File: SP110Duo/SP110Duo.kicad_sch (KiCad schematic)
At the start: 251 parts, among them SW1 RotaryEncoder_Switch, SW10 Switch w/LED, SW100 Switch w/LED, SW101 Switch w/LED, SW102 Switch w/LED, SW103 Switch w/LED, SW104 Switch w/LED, SW105 Switch w/LED, SW106 Switch w/LED, SW107 Switch w/LED, SW108 Switch w/LED, SW109 Switch w/LED, SW11 Switch w/LED, SW110 Switch w/LED, SW12 Switch w/LED, SW13 Switch w/LED, SW14 Switch w/LED, SW15 Switch w/LED, SW16 Switch w/LED, SW17 Switch w/LED, SW18 Switch w/LED, SW19 Switch w/LED, SW2 Switch w/LED, SW20 Switch w/LED, SW21 Switch w/LED, SW22 Switch w/LED, SW23 Switch w/LED, SW24 Switch w/LED, SW25 Switch w/LED, SW26 Switch w/LED, SW27 Switch w/LED, SW28 Switch w/LED, SW29 Switch w/LED, SW3 Switch w/LED, SW30 Switch w/LED, SW31 Switch w/LED, SW32 Switch w/LED, SW33 Switch w/LED, SW34 Switch w/LED, SW35 Switch w/LED, SW36 Switch w/LED, SW37 Switch w/LED, SW38 Switch w/LED, SW39 Switch w/LED, SW4 Switch w/LED, SW40 Switch w/LED, SW41 Switch w/LED, SW42 Switch w/LED, SW43 Switch w/LED, SW44 Switch w/LED, SW45 Switch w/LED, SW46 Switch w/LED, SW47 Switch w/LED, SW48 Switch w/LED, SW49 Switch w/LED, SW5 Switch w/LED, SW50 Switch w/LED, SW51 Switch w/LED, SW52 Switch w/LED, SW53 Switch w/LED, SW54 Switch w/LED, SW55 Switch w/LED, SW56 Switch w/LED, SW57 Switch w/LED, SW58 Switch w/LED, SW59 Switch w/LED, SW6 Switch w/LED, SW60 Switch w/LED, SW61 RotaryEncoder_Switch, SW62 Switch w/LED, SW63 Switch w/LED, SW64 Switch w/LED, SW65 Switch w/LED, SW66 Switch w/LED, SW67 Switch w/LED, SW68 Switch w/LED, SW69 Switch w/LED, SW7 Switch w/LED, SW70 Switch w/LED, SW71 Switch w/LED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

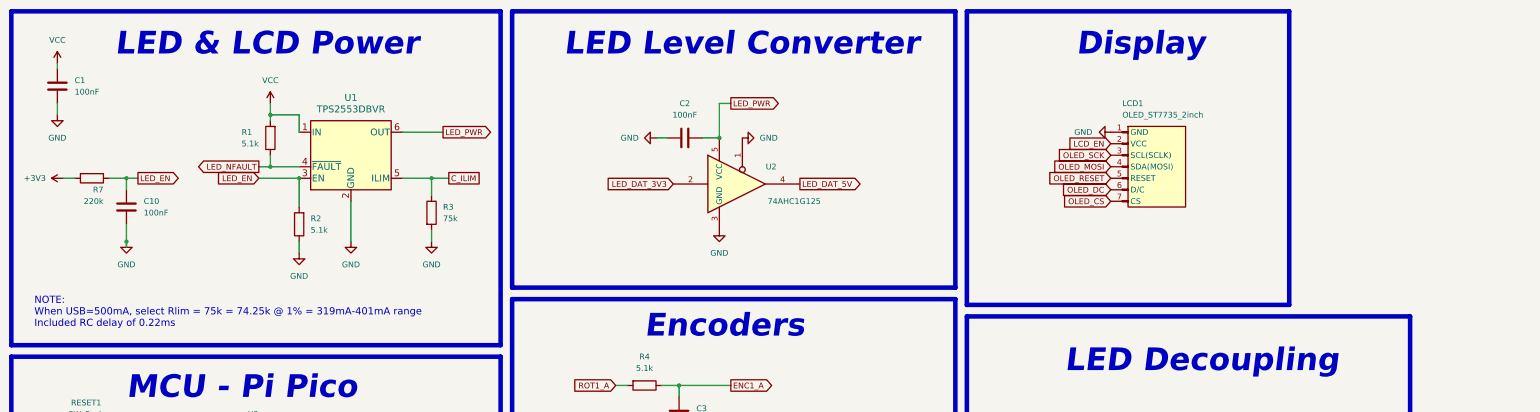
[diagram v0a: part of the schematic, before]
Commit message: Modify diode footprint, add LCD PWR circuit
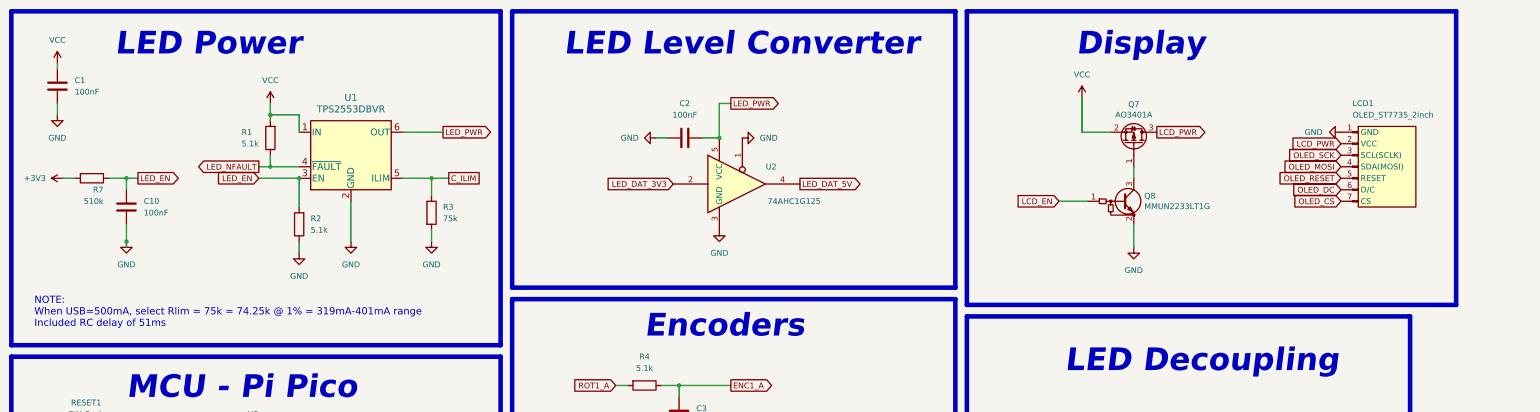
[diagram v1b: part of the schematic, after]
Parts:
- added Q7: AO3401A, Package_TO_SOT_SMD:SOT-23-3, symbol Transistor_FET:AO3401A
- added Q8: MMUN2233LT1G, Package_TO_SOT_SMD:SOT-23-3, symbol Device:Q_NPN_BEC_BRT
- D1, D10, D100, D101, D102, D103, D104, D105, D106, D107, D108, D109, D11, D110, D12, D13, D14, D15, D16, D17, D18, D19, D2, D20, D21, D22, D23, D24, D25, D26, D27, D28, D29, D3, D30, D31, D32, D33, D34, D35, D36, D37, D38, D39, D4, D40, D41, D42, D43, D44, D45, D46, D47, D48, D49, D5, D50, D51, D52, D53, D54, D55, D56, D57, D58, D59, D6, D60, D61, D62, D63, D64, D65, D66, D67, D68, D69, D7, D70, D71, D72, D73, D74, D75, D76, D77, D78, D79, D8, D80, D81, D82, D83, D84, D85, D86, D87, D88, D89, D9, D90, D91, D92, D93, D94, D95, D96, D97, D98, D99: footprint KeebLib:SOD-123F -> Diode_SMD:D_SOD-123F
- R7: value 220k -> 510k
- U3: footprint KeebLib:Raspberry_Pi_Pico_Flipped_No_Pads -> KeebLib:Raspberry_Pi_Pico
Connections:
- net GND: now also Q8.2 (E)
- net LCD_EN: now also Q8.1 (B); no longer LCD1.2 (VCC)
- net VCC: now also Q7.2 (S)
- new net: Q7.1 (G), Q8.3 (C)
- new net LCD_PWR: LCD1.2 (VCC), Q7.3 (D)
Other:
- note added: "LED Power"
- note added: "NOTE: When USB=500mA, select Rlim = 75k = 74.25k @ 1% = 319mA-401mA range Included RC delay of 51ms"
- note removed: "LED & LCD Power"
- note removed: "NOTE: When USB=500mA, select Rlim = 75k = 74.25k @ 1% = 319mA-401mA range Included RC delay of 0.22ms"
- moved on the sheet: LCD1

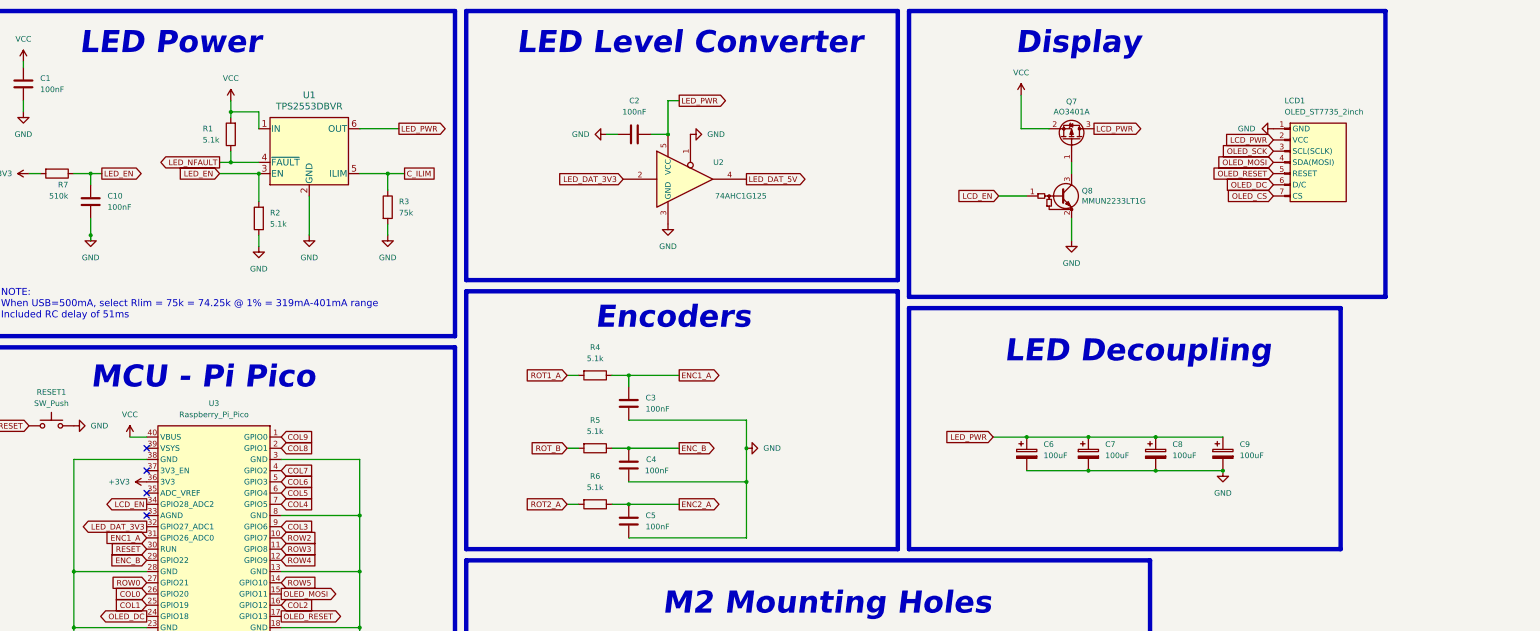
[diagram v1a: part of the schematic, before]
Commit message: Update decoupling
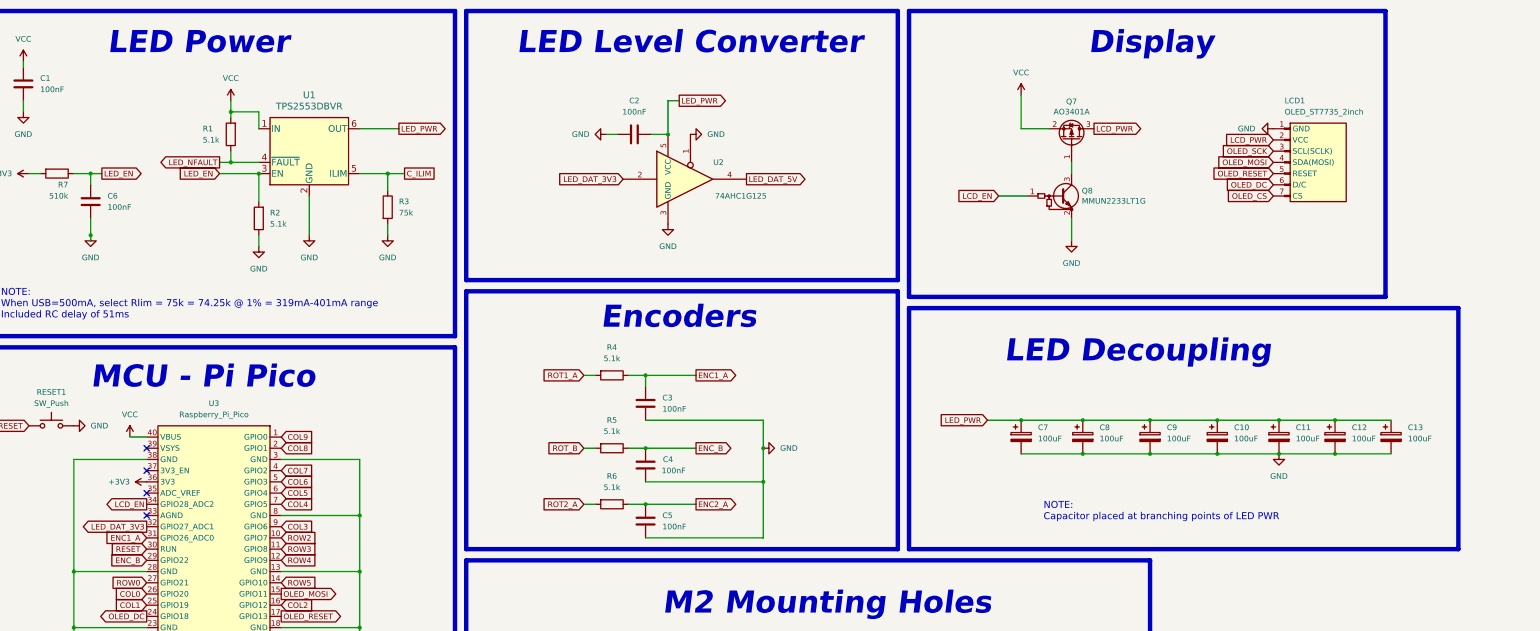
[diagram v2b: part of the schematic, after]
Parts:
- added C11, C12, C13: 100uF, Capacitor_Tantalum_SMD:CP_EIA-6032-15_Kemet-U_Pad2.25x2.35mm_HandSolder, symbol Device:C_Polarized
- renumbered C9 to C10, C10 to C6, C6 to C7, C7 to C8, C8 to C9
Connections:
- net GND: now also C11.2, C12.2, C13.2
- net LED_PWR: now also C11.1, C12.1, C13.1
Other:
- note added: "NOTE: Capacitor placed at branching points of LED PWR"
- moved on the sheet: C10, C3, C4, C5, C7, C8, C9, R4, R5, R6

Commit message: add footprints for LCDs
add autosave to gitignore
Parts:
- added LCD2: LCD-ST7789-2in, LCD-ST7789-2in, symbol SP110DUO:LCD-ST7789-2in
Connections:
- net GND: now also LCD2.1 (Pin_1)
- net LCD_EN: no longer U3.34 (GPIO28_ADC2)
- net LCD_PWR: now also LCD2.2 (Pin_2); no longer LCD1.2 (VCC)
- net OLED_CS renamed LCD_CS
- net LCD_CS: now also LCD2.7 (Pin_7)
- net OLED_DC renamed LCD_DC
- net LCD_DC: now also LCD2.6 (Pin_6)
- net OLED_MOSI renamed LCD_MOSI
- net LCD_MOSI: now also LCD2.4 (Pin_4)
- net OLED_RESET renamed LCD_RESET
- net LCD_RESET: now also LCD2.5 (Pin_5)
- net OLED_SCK renamed LCD_SCK
- net LCD_SCK: now also LCD2.3 (Pin_3)
- new net LCD_BL_PWM: LCD2.8 (Pin_8), U3.34 (GPIO28_ADC2)

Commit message: PCB rev01 update
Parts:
- removed LCD1: OLED_ST7735_2inch, KeebLib:OLED_ST7735_2inch, symbol KeebLib:OLED_ST7735_2inch
- removed Q7: AO3401A, Package_TO_SOT_SMD:SOT-23-3, symbol Transistor_FET:AO3401A
- removed Q8: MMUN2233LT1G, Package_TO_SOT_SMD:SOT-23-3, symbol Device:Q_NPN_BEC_BRT
- C6: value 100nF -> 4.7uF
- LCD1: renamed from LCD2; footprint LCD-ST7789-2in -> SP110Duo:LCD-ST7789-2in
- R7: value 510k -> 10k
- U3: footprint KeebLib:Raspberry_Pi_Pico -> ScottoKeebs_MCU:Raspberry_Pi_Pico
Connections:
- net LCD_PWR is gone; now on net +3V3: LCD1.2 (Pin_2)
- net COL0: now also U3.31 (GPIO26_ADC0); no longer U3.26 (GPIO20)
- net ENC1_A: no longer U3.31 (GPIO26_ADC0)
- net ENC2_A: no longer U3.21 (GPIO16)
- net ENC_B: no longer U3.29 (GPIO22)
- net GND: no longer U3.42 (GND)
- net LCD_BL_PWM: now also U3.21 (GPIO16); no longer U3.34 (GPIO28_ADC2)
- net LED_DAT_3V3: now also U3.34 (GPIO28_ADC2); no longer U3.32 (GPIO27_ADC1)
- net ROW0: now also U3.32 (GPIO27_ADC1); no longer U3.27 (GPIO21)
- net ROW1: no longer U3.20 (GPIO15)
- net LCD_MOSI: no longer names the net of U3.15 (GPIO11)
- net LCD_MOSI: no longer LCD1.4 (Pin_4)
- net LCD_SCK renamed LCD_SCK/SCL
- new net LCD_MOSI/SDA: LCD1.4 (Pin_4), U3.20 (GPIO15)
- no-connect marks 7 -> 8
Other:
- note added: "LED Delay Timer"
- note added: "NOTE: When USB=500mA, select Rlim = 75k = 74.25k @ 1% = 319mA-401mA range"
- note added: "Simple RC delay used to send on signals to LED current limiter & LED Power circuit ~47ms to reach 63% of 3V3"
- note removed: "NOTE: When USB=500mA, select Rlim = 75k = 74.25k @ 1% = 319mA-401mA range Included RC delay of 51ms"
- moved on the sheet: C10, C11, C12, C13, C3, C4, C5, C6, C7, C8, C9, LCD1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

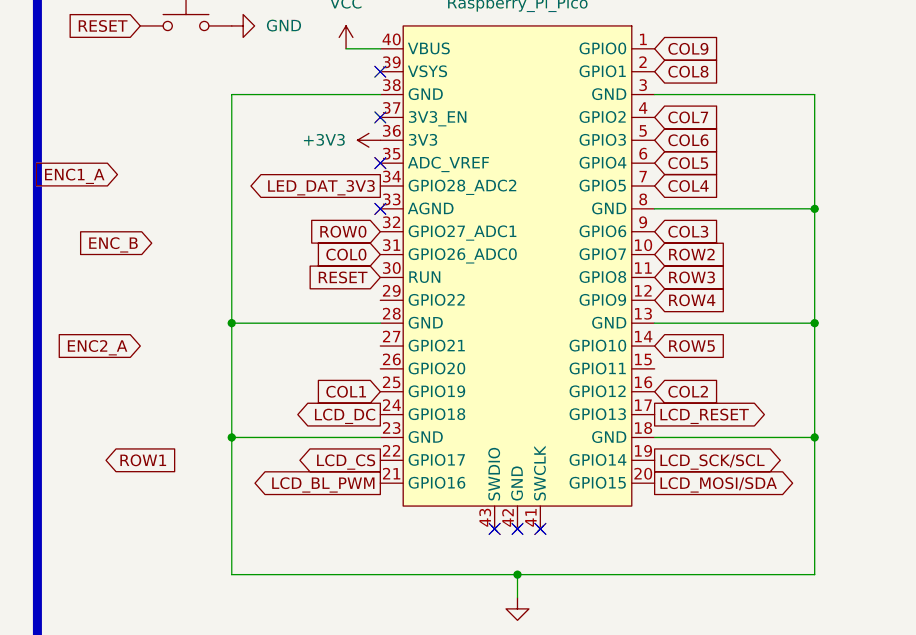
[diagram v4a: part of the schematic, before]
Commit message: Align schematic to PCB
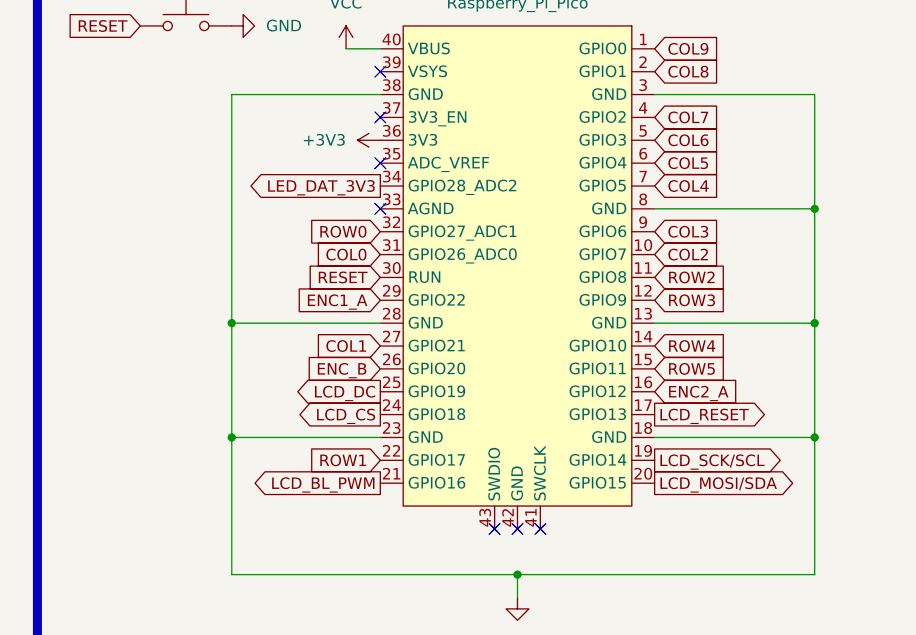
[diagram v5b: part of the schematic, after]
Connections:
- net COL1: now also U3.27 (GPIO21); no longer U3.25 (GPIO19)
- net COL2: now also U3.10 (GPIO7); no longer U3.16 (GPIO12)
- net ENC1_A: now also U3.29 (GPIO22)
- net ENC2_A: now also U3.16 (GPIO12)
- net ENC_B: now also U3.26 (GPIO20)
- net LCD_CS: now also U3.24 (GPIO18); no longer U3.22 (GPIO17)
- net LCD_DC: now also U3.25 (GPIO19); no longer U3.24 (GPIO18)
- net ROW1: now also U3.22 (GPIO17)
- net ROW2: now also U3.11 (GPIO8); no longer U3.10 (GPIO7)
- net ROW3: now also U3.12 (GPIO9); no longer U3.11 (GPIO8)
- net ROW4: now also U3.14 (GPIO10); no longer U3.12 (GPIO9)
- net ROW5: now also U3.15 (GPIO11); no longer U3.14 (GPIO10)

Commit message: update traces
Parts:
- added H10: MountingHole, MountingHole:MountingHole_2.2mm_M2_DIN965_Pad, symbol Mechanical:MountingHole
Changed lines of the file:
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@@
+    )
+  )
+  (symbol (lib_id "Mechanical:MountingHole") (at 347.98 176.53 0) (unit 1)
+    (in_bom yes) (on_board yes) (dnp no) (fields_autoplaced)
+    (property "Reference" "H10" (at 350.52 175.26 0)
+      (effects (font (size 1.27 1.27)) (justify left))
+    )
+    (property "Value" "MountingHole" (at 350.52 177.8 0)
+      (effects (font (size 1.27 1.27)) (justify left))
+    )
+    (property "Footprint" "MountingHole:MountingHole_2.2mm_M2_DIN965_Pad" (at 347.98 176.53 0)
+      (effects (font (size 1.27 1.27)) hide)
+    )
+    (property "Datasheet" "~" (at 347.98 176.53 0)
+      (effects (font (size 1.27 1.27)) hide)
+    )
+    (instances
+      (project "SP110Duo"
+        (path "/9efe463e-e9e8-4c7d-9e2c-b657456ce19f"
+          (reference "H10") (unit 1)
+        )
+      )
     )
   )
@@
   )
   (symbol (lib_id "Device:C") (at 116.84 35.56 180) (unit 1)
-    (in_bom yes) (on_board yes) (dnp no) (fields_autoplaced)
+    (in_bom yes) (on_board yes) (dnp no)
     (property "Reference" "C1" (at 120.65 34.29 0)
       (effects (font (size 1.27 1.27)) (justify right))
